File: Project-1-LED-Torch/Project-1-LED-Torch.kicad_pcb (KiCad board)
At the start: 2 copper layers, 61.5 x 25.1 mm, 5 parts, among them SW1 SW_DPDT_x2

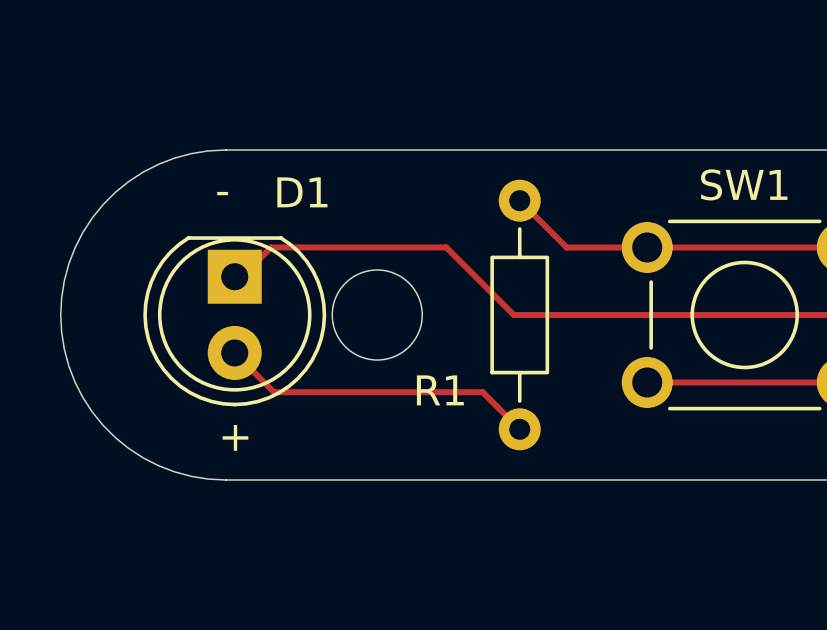
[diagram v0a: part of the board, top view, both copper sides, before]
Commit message: bugfix: add real mounting hole - update PCB layout design, step 9, outline and constraints (9.2. define mounting holes)
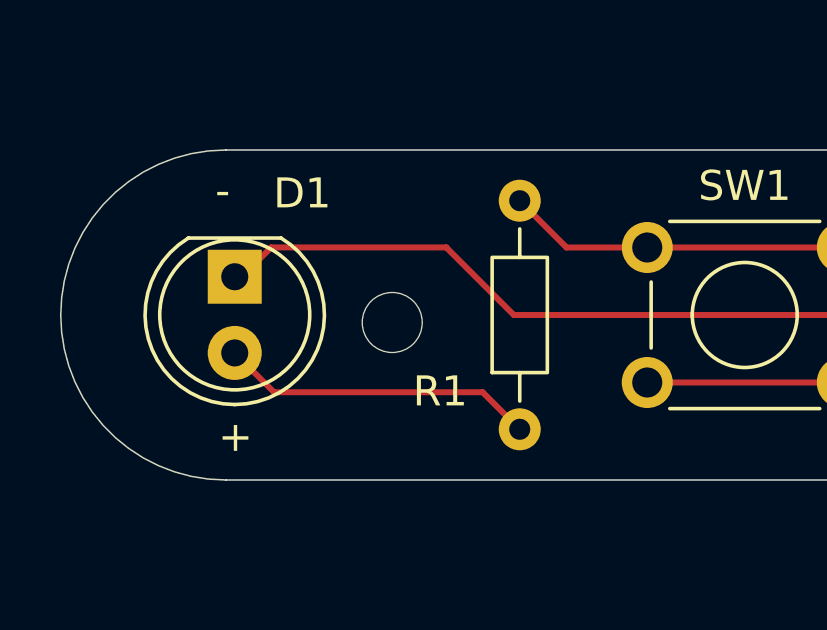
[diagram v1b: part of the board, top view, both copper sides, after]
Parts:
- added REF**: MountingHole_2mm, MountingHole:MountingHole_2mm, F.Cu at (65.0, 113.5)
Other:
- outline, holes or cut-outs redrawn
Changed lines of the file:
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@@
 			(plot_on_all_layers_selection 0x00000000_00000000_00000000_00000000)
 			(disableapertmacros no)
-			(usegerberextensions no)
+			(usegerberextensions yes)
 			(usegerberattributes yes)
 			(usegerberadvancedattributes yes)
@@
 			(outputformat 1)
 			(mirror no)
-			(drillshape 1)
+			(drillshape 0)
 			(scaleselection 1)
-			(outputdirectory "")
+			(outputdirectory "Gerber files for LED Torch/")
 		)
 	)
@@
 			)
 		)
+	)
+	(footprint "MountingHole:MountingHole_2mm"
+		(locked yes)
+		(layer "F.Cu")
+		(at 65 113.5)
+		(descr "Mounting Hole 2mm, no annular, generated by kicad-footprint-generator mountinghole.py")
+		(tags "mountinghole")
+		(property "Reference" "REF**"
+			(at 0 -2.95 0)
+			(layer "F.SilkS")
+			(hide yes)
+			(effects
+				(font
+					(size 1 1)
+					(thickness 0.15)
+				)
+			)
+		)
+		(property "Value" "MountingHole_2mm"
+			(at 0 2.95 0)
+			(layer "F.Fab")
+			(hide yes)
+			(effects
+				(font
+					(size 1 1)
+					(thickness 0.15)
+				)
+			)
+		)
+		(property "Datasheet" ""
+			(at 0 0 0)
+			(layer "F.Fab")
+			(hide yes)
+			(effects
+				(font
+					(size 1.27 1.27)
+				)
+			)
+		)
+		(property "Description" ""
+			(at 0 0 0)
+			(layer "F.Fab")
+			(hide yes)
+			(effects
+				(font
+					(size 1.27 1.27)
+				)
+			)
+		)
+		(property "KiLib_Generator" "mounting_hardware/mounting_hole"
+			(at 0 0 0)
+			(layer "F.SilkS")
+			(hide yes)
+			(effects
+				(font
+					(size 1 1)
+					(thickness 0.15)
+				)
+			)
+		)
+		(attr through_hole board_only exclude_from_pos_files exclude_from_bom)
+		(duplicate_pad_numbers_are_jumpers no)
+		(fp_circle
+			(center 0 0)
+			(end 2 0)
+			(stroke
+				(width 0.15)
+				(type solid)
+			)
+			(fill no)
+			(layer "Cmts.User")
+		)
+		(fp_circle
+			(center 0 0)
+			(end 2.25 0)
+			(stroke
+				(width 0.05)
+				(type solid)
+			)
+			(fill no)
+			(layer "F.CrtYd")
+		)
+		(fp_text user "${REFERENCE}"
+			(at 0 0 0)
+			(layer "F.Fab")
+			(effects
+				(font
+					(size 1 1)
+					(thickness 0.15)
+				)
+			)
+		)
+		(pad "" np_thru_hole circle
+			(at 0 0)
+			(size 2 2)
+			(drill 2)
+			(layers "*.Cu" "*.Mask")
+		)
+		(embedded_fonts no)
 	)
 	(footprint "Battery:BatteryHolder_Keystone_1058_1x2032"
@@
 		(layer "Edge.Cuts")
 	)
-	(gr_circle
-		(center 64.5 113.25)
-		(end 66 113.25)
-		(stroke
-			(width 0.05)
-			(type default)
-		)
-		(fill no)
-		(layer "Edge.Cuts")
-	)
 	(gr_arc
 		(start 87.45 107.75)
@@
 	)
 	(segment
+		(start 68.014 115.824)
+		(end 69.25 117.06)
+		(width 0.2)
+		(layer "F.Cu")
+		(net "/LED_anode")
+	)
+	(segment
+		(start 61.059 115.824)
+		(end 68.014 115.824)
+		(width 0.2)
+		(layer "F.Cu")
+		(net "/LED_anode")
+	)
+	(segment
+		(start 59.75 114.515)
+		(end 61.059 115.824)
+		(width 0.2)
+		(layer "F.Cu")
+		(net "/LED_anode")
+	)
+	(segment
+		(start 73.5 111)
+		(end 80 111)
+		(width 0.2)
+		(layer "F.Cu")
+		(net "Net-(SW1A-A)")
+	)
+	(segment
+		(start 73.5 111)
+		(end 70.81 111)
+		(width 0.2)
+		(layer "F.Cu")
+		(net "Net-(SW1A-A)")
+	)
+	(segment
+		(start 70.81 111)
+		(end 69.25 109.44)
+		(width 0.2)
+		(layer "F.Cu")
+		(net "Net-(SW1A-A)")
+	)
+	(segment
 		(start 73.5 115.5)
 		(end 80 115.5)
@@
 		(net "/Battery_positive")
 	)
-	(segment
-		(start 68.014 115.824)
-		(end 69.25 117.06)
-		(width 0.2)
-		(layer "F.Cu")
-		(net "/LED_anode")
-	)
-	(segment
-		(start 61.059 115.824)
-		(end 68.014 115.824)
-		(width 0.2)
-		(layer "F.Cu")
-		(net "/LED_anode")
-	)
-	(segment
-		(start 59.75 114.515)
-		(end 61.059 115.824)
-		(width 0.2)
-		(layer "F.Cu")
-		(net "/LED_anode")
-	)
-	(segment
-		(start 73.5 111)
-		(end 80 111)
-		(width 0.2)
-		(layer "F.Cu")
-		(net "Net-(SW1A-A)")
-	)
-	(segment
-		(start 73.5 111)
-		(end 70.81 111)
-		(width 0.2)
-		(layer "F.Cu")
-		(net "Net-(SW1A-A)")
-	)
-	(segment
-		(start 70.81 111)
-		(end 69.25 109.44)
-		(width 0.2)
-		(layer "F.Cu")
-		(net "Net-(SW1A-A)")
-	)
 	(embedded_fonts no)
